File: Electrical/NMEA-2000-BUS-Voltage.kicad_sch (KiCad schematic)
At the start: 12 parts, among them J1 Conn_01x07, U1 WeMos_D1_mini, U2 LM7805_TO220, U3 SN65HVD230-Module

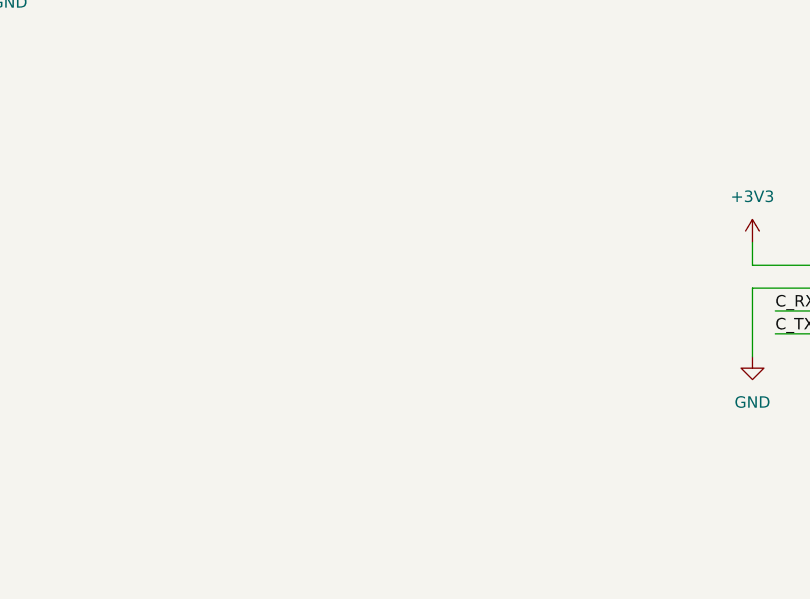
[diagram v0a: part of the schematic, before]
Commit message: Added BMP280-Module to Schematic
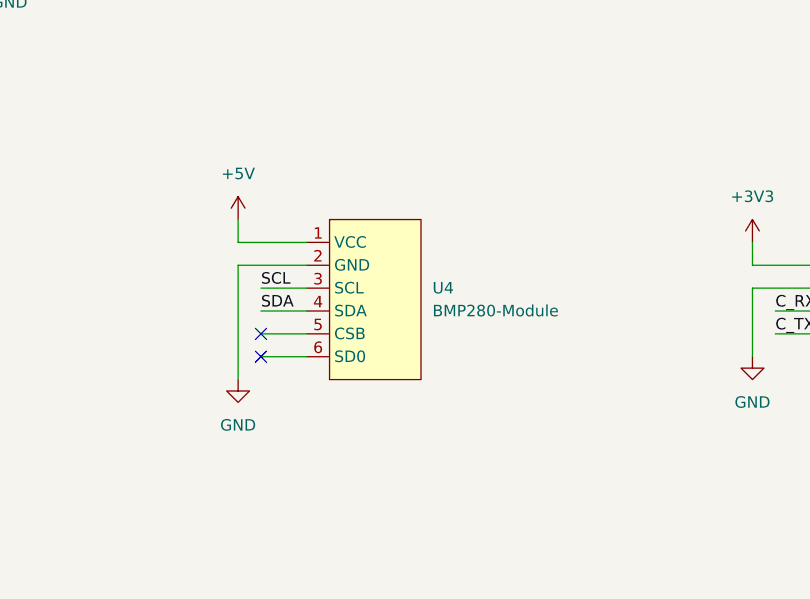
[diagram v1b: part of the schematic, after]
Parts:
- added U4: BMP280-Module, symbol BMP280-Module:BMP280-Module
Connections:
- net +5V: now also U4.1 (VCC)
- net GND: now also U4.2 (GND)
- new net SCL: U4.3 (SCL)
- new net SDA: U4.4 (SDA)
- no-connect marks 4 -> 6
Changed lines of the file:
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@@
   (no_connect (at 34.29 87.63))
   (no_connect (at 64.77 97.79))
+  (no_connect (at 124.46 157.48))
+  (no_connect (at 124.46 154.94))
   (wire (pts (xy 34.29 87.63) (xy 39.37 87.63))
     (stroke (width 0) (type default))
@@
     (stroke (width 0) (type default))
   )
+  (wire (pts (xy 121.92 142.24) (xy 121.92 144.78))
+    (stroke (width 0) (type default))
+  )
   (wire (pts (xy 210.82 82.55) (xy 210.82 87.63))
     (stroke (width 0) (type default))
@@
     (stroke (width 0) (type default))
   )
+  (wire (pts (xy 121.92 147.32) (xy 121.92 160.02))
+    (stroke (width 0) (type default))
+  )
   (wire (pts (xy 64.77 87.63) (xy 59.69 87.63))
     (stroke (width 0) (type default))
   )
+  (wire (pts (xy 129.54 147.32) (xy 121.92 147.32))
+    (stroke (width 0) (type default))
+  )
   (wire (pts (xy 96.52 90.17) (xy 96.52 92.71))
     (stroke (width 0) (type default))
@@
     (stroke (width 0) (type default))
   )
+  (wire (pts (xy 129.54 144.78) (xy 121.92 144.78))
+    (stroke (width 0) (type default))
+  )
   (wire (pts (xy 186.69 99.06) (xy 186.69 96.52))
     (stroke (width 0) (type default))
@@
     (stroke (width 0) (type default))
   )
+  (wire (pts (xy 124.46 149.86) (xy 129.54 149.86))
+    (stroke (width 0) (type default))
+  )
+  (wire (pts (xy 124.46 157.48) (xy 129.54 157.48))
+    (stroke (width 0) (type default))
+  )
   (wire (pts (xy 213.36 92.71) (xy 218.44 92.71))
     (stroke (width 0) (type default))
@@
     (stroke (width 0) (type default))
   )
+  (wire (pts (xy 124.46 152.4) (xy 129.54 152.4))
+    (stroke (width 0) (type default))
+  )
   (wire (pts (xy 218.44 95.25) (xy 213.36 95.25))
     (stroke (width 0) (type default))
@@
   )
   (wire (pts (xy 179.07 149.86) (xy 179.07 157.48))
+    (stroke (width 0) (type default))
+  )
+  (wire (pts (xy 124.46 154.94) (xy 129.54 154.94))
     (stroke (width 0) (type default))
   )
@@
     (effects (font (size 1.27 1.27)) (justify left bottom))
   )
+  (label "SDA" (at 124.46 152.4 0) (fields_autoplaced)
+    (effects (font (size 1.27 1.27)) (justify left bottom))
+  )
   (label "C_RX" (at 30.48 151.13 0) (fields_autoplaced)
+    (effects (font (size 1.27 1.27)) (justify left bottom))
+  )
+  (label "SCL" (at 124.46 149.86 0) (fields_autoplaced)
     (effects (font (size 1.27 1.27)) (justify left bottom))
   )
@@
     )
   )
+  (symbol (lib_id "power:+5V") (at 121.92 142.24 0) (unit 1)
+    (in_bom yes) (on_board yes) (dnp no) (fields_autoplaced)
+    (property "Reference" "#PWR014" (at 121.92 146.05 0)
+      (effects (font (size 1.27 1.27)) hide)
+    )
+    (property "Value" "+5V" (at 121.92 137.16 0)
+      (effects (font (size 1.27 1.27)))
+    )
+    (property "Footprint" "" (at 121.92 142.24 0)
+      (effects (font (size 1.27 1.27)) hide)
+    )
+    (property "Datasheet" "" (at 121.92 142.24 0)
+      (effects (font (size 1.27 1.27)) hide)
+    )
+    (pin "1")
+    (instances
+      (project "NMEA-2000-BUS-Voltage"
+        (path "/2ad9a196-bb2f-4407-b356-e110a1476183"
+          (reference "#PWR014") (unit 1)
+        )
+      )
+    )
+  )
   (symbol (lib_id "power:GND") (at 213.36 102.87 0) (unit 1)
     (in_bom yes) (on_board yes) (dnp no) (fields_autoplaced)
@@
         (path "/2ad9a196-bb2f-4407-b356-e110a1476183"
           (reference "U3") (unit 1)
+        )
+      )
+    )
+  )
+  (symbol (lib_id "power:GND") (at 121.92 160.02 0) (unit 1)
+    (in_bom yes) (on_board yes) (dnp no) (fields_autoplaced)
+    (property "Reference" "#PWR015" (at 121.92 166.37 0)
+      (effects (font (size 1.27 1.27)) hide)
+    )
+    (property "Value" "GND" (at 121.92 165.1 0)
+      (effects (font (size 1.27 1.27)))
+    )
+    (property "Footprint" "" (at 121.92 160.02 0)
+      (effects (font (size 1.27 1.27)) hide)
+    )
+    (property "Datasheet" "" (at 121.92 160.02 0)
+      (effects (font (size 1.27 1.27)) hide)
+    )
+    (pin "1")
+    (instances
+      (project "NMEA-2000-BUS-Voltage"
+        (path "/2ad9a196-bb2f-4407-b356-e110a1476183"
+          (reference "#PWR015") (unit 1)
         )
       )
@@
         )
       )
+    )
+  )
+  (symbol (lib_id "BMP280-Module:BMP280-Module") (at 137.16 138.43 0) (unit 1)
+    (in_bom yes) (on_board yes) (dnp no) (fields_autoplaced)
+    (property "Reference" "U4" (at 143.51 149.86 0)
+      (effects (font (size 1.27 1.27)) (justify left))
+    )
+    (property "Value" "BMP280-Module" (at 143.51 152.4 0)
+      (effects (font (size 1.27 1.27)) (justify left))
+    )
+    (property "Footprint" "" (at 137.16 138.43 0)
+      (effects (font (size 1.27 1.27)) hide)
+    )
+    (property "Datasheet" "" (at 137.16 138.43 0)
+      (effects (font (size 1.27 1.27)) hide)
+    )
+    (pin "1")
+    (pin "2")
+    (pin "3")
+    (pin "4")
+    (pin "5")
+    (pin "6")
+    (instances
+      (project "NMEA-2000-BUS-Voltage"
+        (path "/2ad9a196-bb2f-4407-b356-e110a1476183"
+          (reference "U4") (unit 1)
+        )
+      )

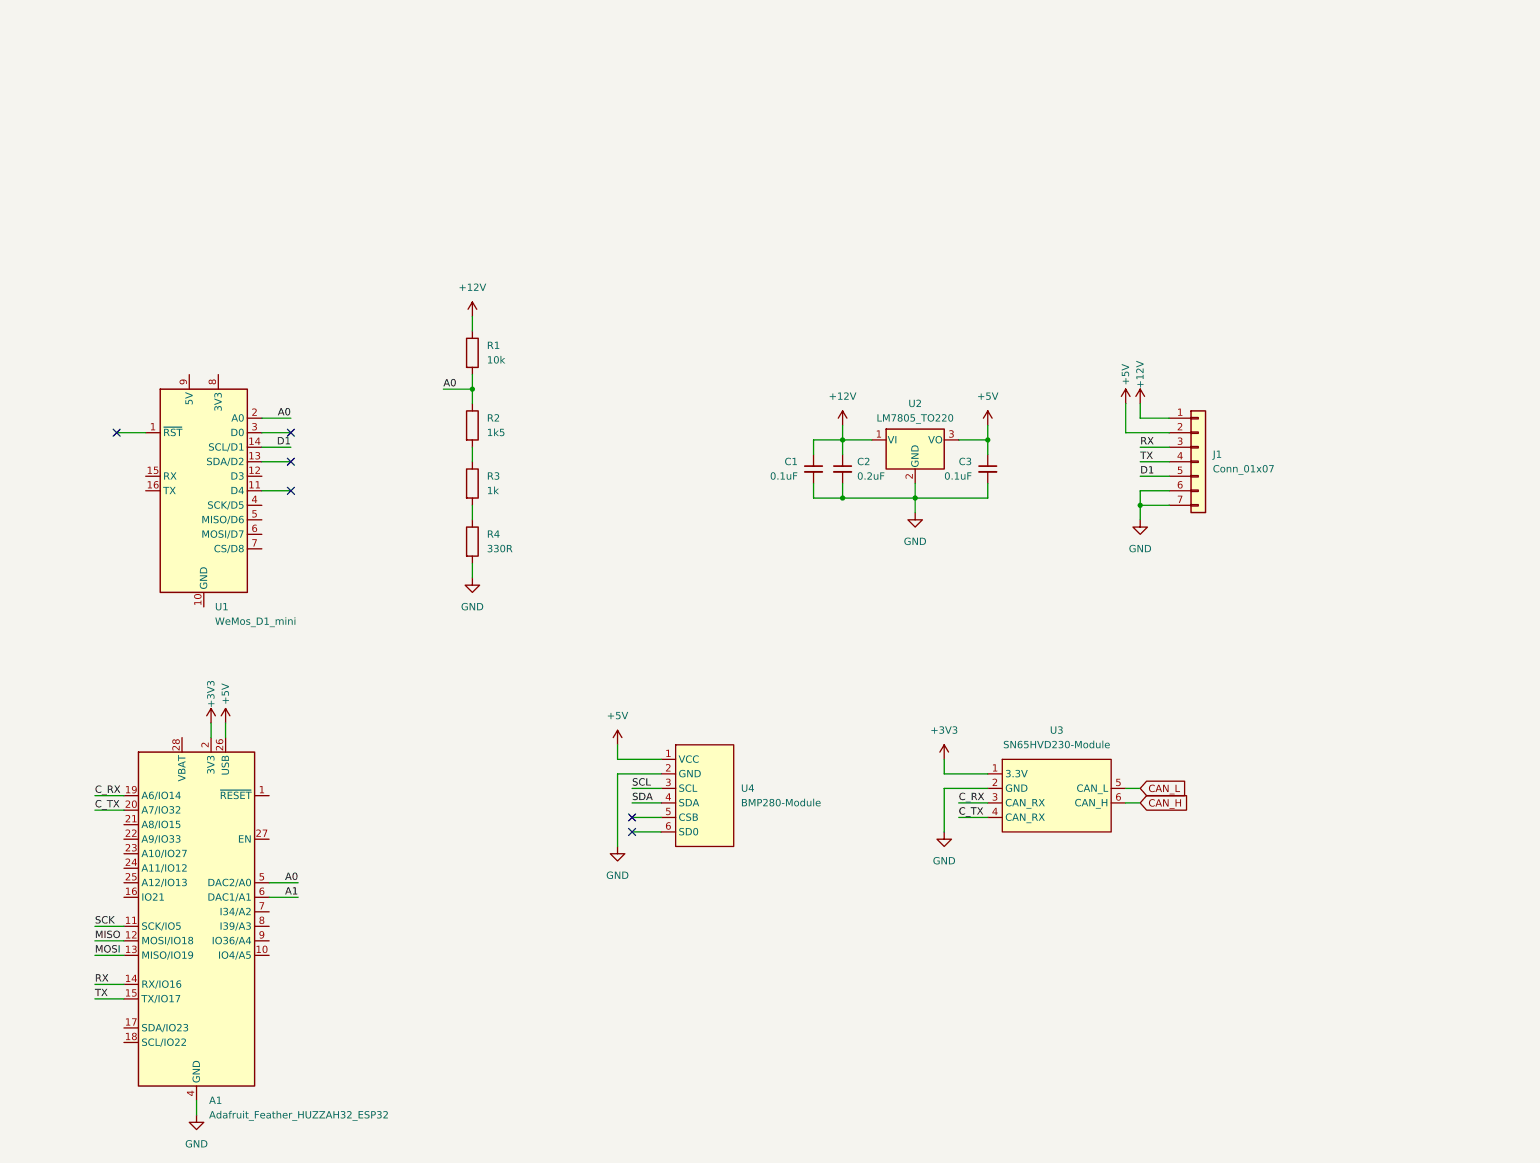
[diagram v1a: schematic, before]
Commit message: Added ACS712-Module to Schematic
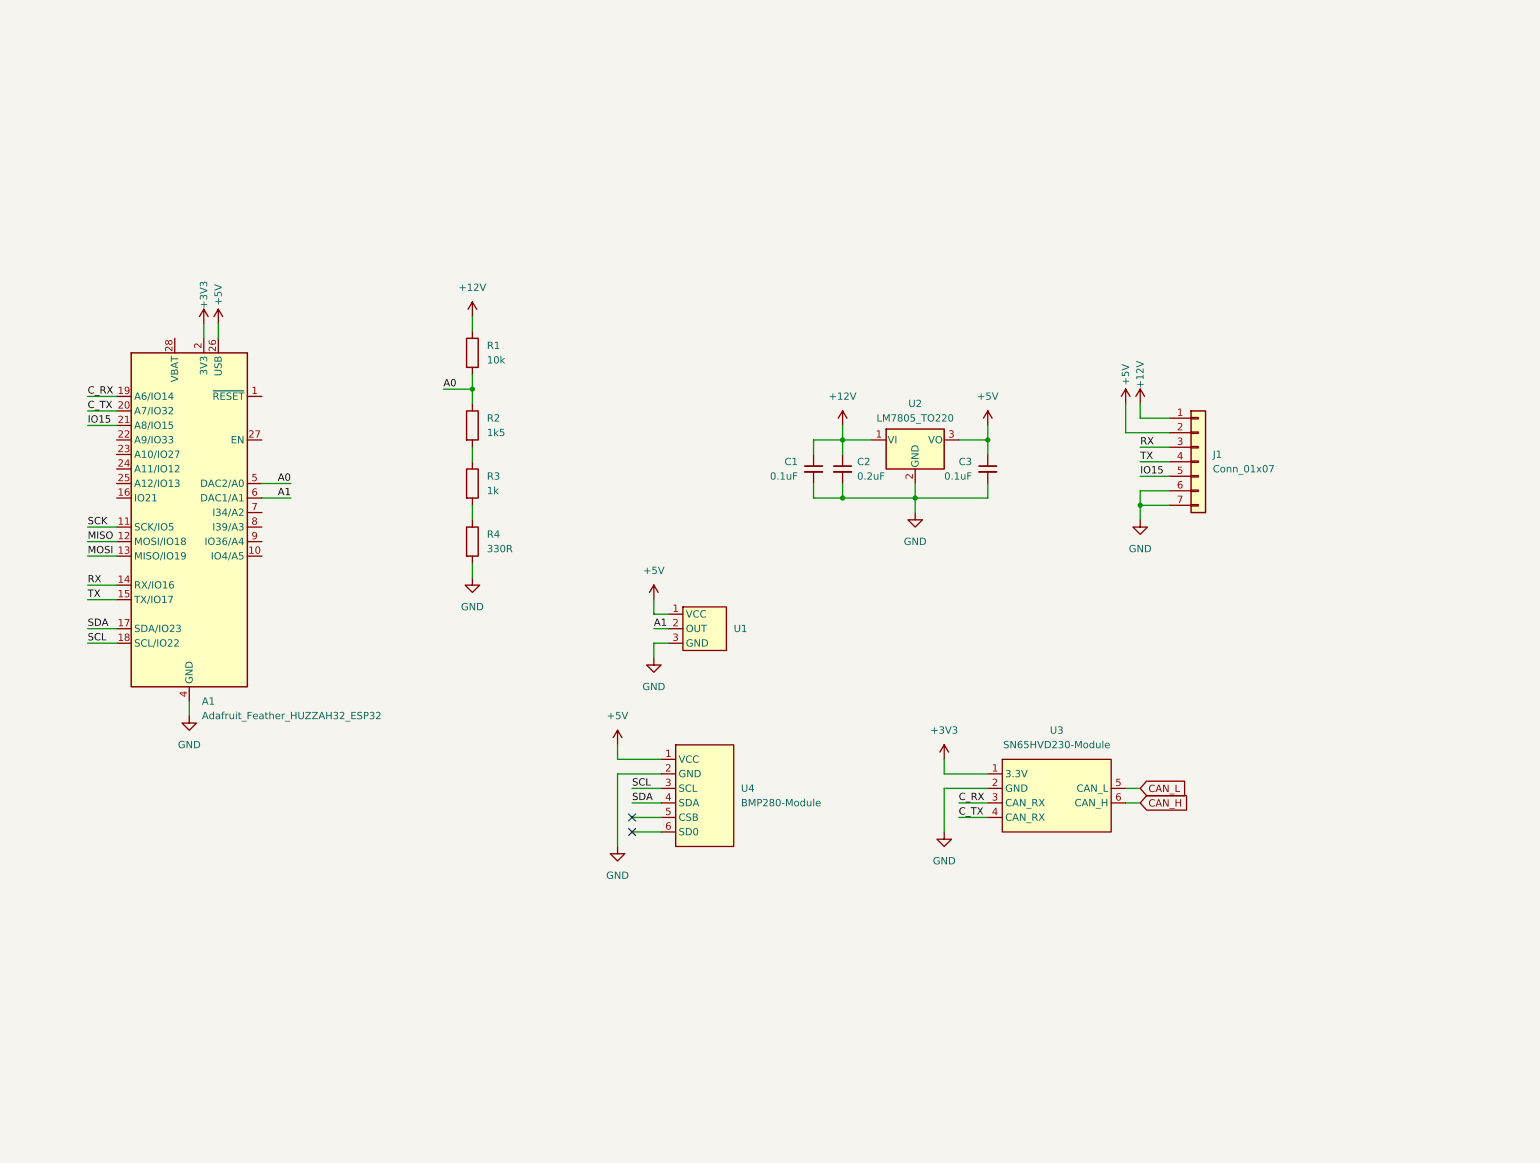
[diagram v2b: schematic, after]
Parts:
- removed U1: WeMos_D1_mini, Module:WEMOS_D1_mini_light, symbol MCU_Module:WeMos_D1_mini
- added U1: ~, symbol ACS712:ACS712-Module
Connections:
- net D1 is gone; now on net IO15: J1.5 (Pin_5)
- net +5V: now also U1.1 (VCC)
- net A1: now also U1.2 (OUT)
- net GND: now also U1.3 (GND)
- net SCL: now also A1.18 (SCL/IO22)
- net SDA: now also A1.17 (SDA/IO23)
- net IO15: now reaches A1.21 (A8/IO15)
- no-connect marks 6 -> 2
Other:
- moved on the sheet: A1

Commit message: Modified Schematic
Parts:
- U1: value ~ -> ACS712-Module
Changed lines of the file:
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@@
-    )
-  )
-  (symbol (lib_id "ACS712:ACS712-Module") (at 135.89 115.57 0) (unit 1)
-    (in_bom yes) (on_board yes) (dnp no) (fields_autoplaced)
-    (property "Reference" "U1" (at 142.24 121.92 0)
-      (effects (font (size 1.27 1.27)) (justify left))
-    )
-    (property "Value" "~" (at 135.89 115.57 0)
-      (effects (font (size 1.27 1.27)))
-    )
-    (property "Footprint" "" (at 135.89 115.57 0)
-      (effects (font (size 1.27 1.27)) hide)
-    )
-    (property "Datasheet" "" (at 135.89 115.57 0)
-      (effects (font (size 1.27 1.27)) hide)
-    )
-    (pin "1")
-    (pin "2")
-    (pin "3")
-    (instances
-      (project "NMEA-2000-BUS-Voltage"
-        (path "/2ad9a196-bb2f-4407-b356-e110a1476183"
-          (reference "U1") (unit 1)
-        )
-      )
     )
   )
@@
         )
       )
+    )
+  )
+  (symbol (lib_id "ACS712:ACS712-Module") (at 142.24 115.57 0) (unit 1)
+    (in_bom yes) (on_board yes) (dnp no) (fields_autoplaced)
+    (property "Reference" "U1" (at 142.24 113.03 0)
+      (effects (font (size 1.27 1.27)))
+    )
+    (property "Value" "ACS712-Module" (at 142.24 115.57 0)
+      (effects (font (size 1.27 1.27)))
+    )
+    (property "Footprint" "" (at 135.89 115.57 0)
+      (effects (font (size 1.27 1.27)) hide)
+    )
+    (property "Datasheet" "" (at 135.89 115.57 0)
+      (effects (font (size 1.27 1.27)) hide)
+    )
+    (pin "1")
+    (pin "2")
+    (pin "3")
+    (pin "4")
+    (pin "5")
+    (instances
+      (project "NMEA-2000-BUS-Voltage"
+        (path "/2ad9a196-bb2f-4407-b356-e110a1476183"
+          (reference "U1") (unit 1)
+        )
+      )

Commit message: Addedd Relay
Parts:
- removed J1: Conn_01x07, symbol Connector_Generic:Conn_01x07
- added K2: RAYEX-L90, Relay_THT:Relay_SPDT_RAYEX-L90, symbol Relay:RAYEX-L90
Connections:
- net +12V: now also K2.11A, K2.11B; no longer C1.1, C2.1, R1.1, U2.1 (VI)
- net GND: now also K2.A2
- net IO15: now also K2.A1
- net +12VA: now reaches U1.4 (I+)
- net +12VA: now also C1.1, C2.1, R1.1, U2.1 (VI), K2.12
- net -12V: now reaches U1.5 (I-)
- no-connect marks 2 -> 3

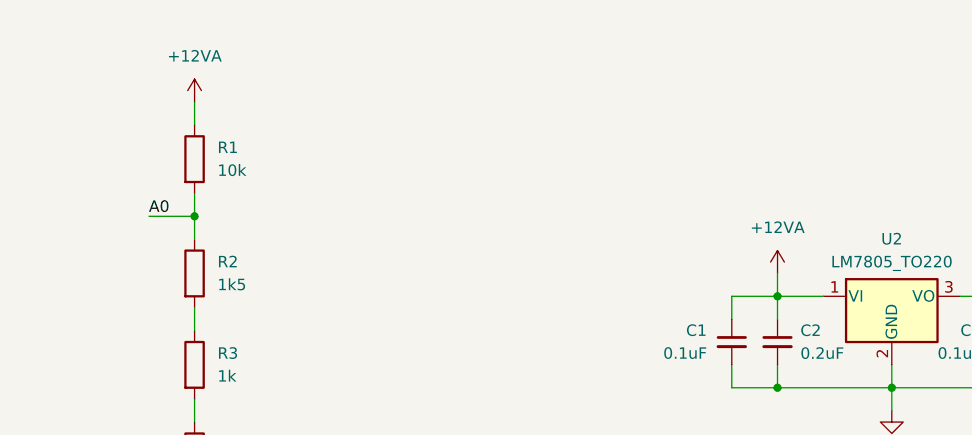
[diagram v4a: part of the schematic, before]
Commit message: Added 12-15V voltageboost
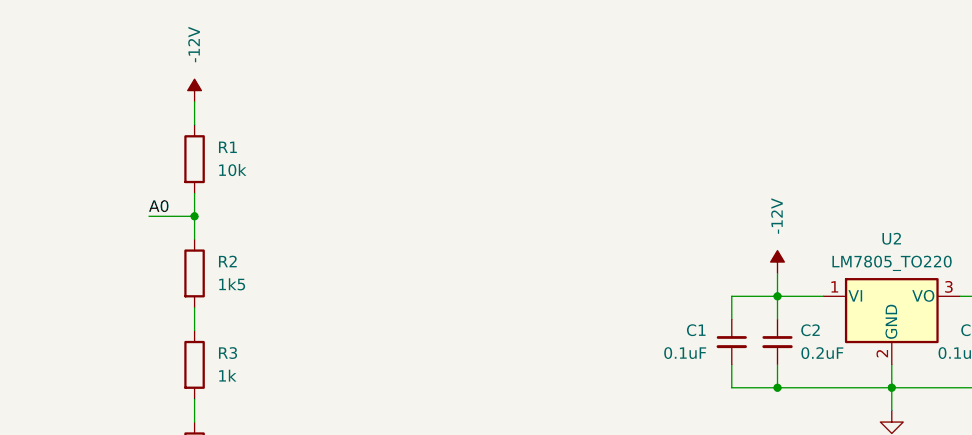
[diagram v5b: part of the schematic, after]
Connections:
- net +12VA: no longer C1.1, C2.1, R1.1, U2.1 (VI)
- net -12V: now also C1.1, C2.1, R1.1, U2.1 (VI)
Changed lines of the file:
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@@
-    )
-  )
-  (symbol (lib_id "power:+12VA") (at 161.29 86.36 0) (unit 1)
-    (in_bom yes) (on_board yes) (dnp no) (fields_autoplaced)
-    (property "Reference" "#PWR07" (at 161.29 90.17 0)
-      (effects (font (size 1.27 1.27)) hide)
-    )
-    (property "Value" "+12VA" (at 161.29 81.28 0)
-      (effects (font (size 1.27 1.27)))
-    )
-    (property "Footprint" "" (at 161.29 86.36 0)
-      (effects (font (size 1.27 1.27)) hide)
-    )
-    (property "Datasheet" "" (at 161.29 86.36 0)
-      (effects (font (size 1.27 1.27)) hide)
-    )
-    (pin "1")
-    (instances
-      (project "NMEA-2000-BUS-Voltage"
-        (path "/2ad9a196-bb2f-4407-b356-e110a1476183"
-          (reference "#PWR07") (unit 1)
-        )
-      )
     )
   )
@@
         (path "/2ad9a196-bb2f-4407-b356-e110a1476183"
           (reference "#PWR02") (unit 1)
+        )
+      )
+    )
+  )
+  (symbol (lib_id "power:-12V") (at 161.29 86.36 0) (unit 1)
+    (in_bom yes) (on_board yes) (dnp no)
+    (property "Reference" "#PWR07" (at 161.29 83.82 0)
+      (effects (font (size 1.27 1.27)) hide)
+    )
+    (property "Value" "-12V" (at 161.29 80.01 90)
+      (effects (font (size 1.27 1.27)))
+    )
+    (property "Footprint" "" (at 161.29 86.36 0)
+      (effects (font (size 1.27 1.27)) hide)
+    )
+    (property "Datasheet" "" (at 161.29 86.36 0)
+      (effects (font (size 1.27 1.27)) hide)
+    )
+    (pin "1")
+    (instances
+      (project "NMEA-2000-BUS-Voltage"
+        (path "/2ad9a196-bb2f-4407-b356-e110a1476183"
+          (reference "#PWR07") (unit 1)
+        )
+      )
+    )
+  )
+  (symbol (lib_id "power:-12V") (at 96.52 67.31 0) (unit 1)
+    (in_bom yes) (on_board yes) (dnp no)
+    (property "Reference" "#PWR04" (at 96.52 64.77 0)
+      (effects (font (size 1.27 1.27)) hide)
+    )
+    (property "Value" "-12V" (at 96.52 60.96 90)
+      (effects (font (size 1.27 1.27)))
+    )
+    (property "Footprint" "" (at 96.52 67.31 0)
+      (effects (font (size 1.27 1.27)) hide)
+    )
+    (property "Datasheet" "" (at 96.52 67.31 0)
+      (effects (font (size 1.27 1.27)) hide)
+    )
+    (pin "1")
+    (instances
+      (project "NMEA-2000-BUS-Voltage"
+        (path "/2ad9a196-bb2f-4407-b356-e110a1476183"
+          (reference "#PWR04") (unit 1)
         )
       )
@@
         )
       )
-    )
-  )
-  (symbol (lib_id "power:+12VA") (at 96.52 67.31 0) (unit 1)
-    (in_bom yes) (on_board yes) (dnp no) (fields_autoplaced)
-    (property "Reference" "#PWR04" (at 96.52 71.12 0)
-      (effects (font (size 1.27 1.27)) hide)
-    )
-    (property "Value" "+12VA" (at 96.52 62.23 0)
-      (effects (font (size 1.27 1.27)))
-    )
-    (property "Footprint" "" (at 96.52 67.31 0)
-      (effects (font (size 1.27 1.27)) hide)
-    )
-    (property "Datasheet" "" (at 96.52 67.31 0)
-      (effects (font (size 1.27 1.27)) hide)
-    )
-    (pin "1")
-    (instances
-      (project "NMEA-2000-BUS-Voltage"
-        (path "/2ad9a196-bb2f-4407-b356-e110a1476183"
-          (reference "#PWR04") (unit 1)
-        )
-      )
